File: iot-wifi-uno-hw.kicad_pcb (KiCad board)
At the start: 2 copper layers, 68.6 x 53.3 mm, 0 parts

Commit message: final schematic
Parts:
- added U1: usb_mini_b, Connectors:USB_Micro-B, F.Cu at (114.3, 74.9)
- added U2: NCP1117ST33T3G_MountingTab, TO_SOT_Packages_SMD:SOT-223, F.Cu at (133.3, 95.9)
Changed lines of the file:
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@@
-(kicad_pcb (version 20160815) (host pcbnew no-vcs-found-undefined)
+(kicad_pcb (version 20160815) (host pcbnew 201611122049+7349~55~ubuntu16.04.1)
   (general
-    (links 0)
-    (no_connects 0)
-    (area 105.969999 29.407502 174.700001 118.439001)
+    (links 6)
+    (no_connects 6)
+    (area 109.471337 58.578471 178.201339 112.068473)
     (thickness 1.6)
     (drawings 949)
     (tracks 0)
     (zones 0)
-    (modules 0)
-    (nets 1)
+    (modules 2)
+    (nets 3)
   )
   (page A4)
@@
   )
   (net 0 "")
+  (net 1 XO)
+  (net 2 "Net-(C3-Pad1)")
   (net_class Default "This is the default net class."
     (clearance 0.2)
@@
     (diff_pair_gap 0.25)
     (diff_pair_width 0.2)
+    (add_net "Net-(C3-Pad1)")
+    (add_net XO)
+  )
+  (module Connectors:USB_Micro-B (layer F.Cu)
+    (at 114.3 74.93 270)
+    (descr "Micro USB Type B Receptacle")
+    (tags "USB USB_B USB_micro USB_OTG")
+    (attr smd)
+    (fp_text reference U1 (at 0 -3.45 270) (layer F.SilkS)
+      (effects (font (size 1 1) (thickness 0.15)))
+    )
+    (fp_text value usb_mini_b (at 0 4.8 270) (layer F.Fab)
+      (effects (font (size 1 1) (thickness 0.15)))
+    )
+    (fp_line (start -4.3509 3.81746) (end -4.3509 -2.58754) (layer F.SilkS) (width 0.15))
+    (fp_line (start 4.3491 2.58746) (end -4.3509 2.58746) (layer F.SilkS) (width 0.15))
+    (fp_line (start 4.3491 -2.58754) (end 4.3491 3.81746) (layer F.SilkS) (width 0.15))
+    (fp_line (start -4.3509 -2.58754) (end 4.3491 -2.58754) (layer F.SilkS) (width 0.15))
+    (fp_line (start -4.3509 3.81746) (end 4.3491 3.81746) (layer F.SilkS) (width 0.15))
+    (fp_line (start -4.6 4.05) (end -4.6 -2.8) (layer F.CrtYd) (width 0.05))
+    (fp_line (start 4.6 4.05) (end -4.6 4.05) (layer F.CrtYd) (width 0.05))
+    (fp_line (start 4.6 -2.8) (end 4.6 4.05) (layer F.CrtYd) (width 0.05))
+    (fp_line (start -4.6 -2.8) (end 4.6 -2.8) (layer F.CrtYd) (width 0.05))
+    (pad 6 thru_hole oval (at 3.4991 1.13746) (size 1.55 1) (drill oval 1.15 0.5) (layers *.Cu *.Mask)
+      (net 1 XO))
+    (pad 6 thru_hole oval (at -3.5009 1.13746) (size 1.55 1) (drill oval 1.15 0.5) (layers *.Cu *.Mask)
+      (net 1 XO))
+    (pad 6 thru_hole oval (at 2.4991 -1.56254) (size 0.95 1.25) (drill oval 0.55 0.85) (layers *.Cu *.Mask)
+      (net 1 XO))
+    (pad 6 thru_hole oval (at -2.5009 -1.56254) (size 0.95 1.25) (drill oval 0.55 0.85) (layers *.Cu *.Mask)
+      (net 1 XO))
+    (pad 5 smd rect (at 1.2991 -1.56254) (size 1.35 0.4) (layers F.Cu F.Paste F.Mask)
+      (net 1 XO))
+    (pad 4 smd rect (at 0.6491 -1.56254) (size 1.35 0.4) (layers F.Cu F.Paste F.Mask))
+    (pad 3 smd rect (at -0.0009 -1.56254) (size 1.35 0.4) (layers F.Cu F.Paste F.Mask))
+    (pad 2 smd rect (at -0.6509 -1.56254) (size 1.35 0.4) (layers F.Cu F.Paste F.Mask))
+    (pad 1 smd rect (at -1.3009 -1.56254) (size 1.35 0.4) (layers F.Cu F.Paste F.Mask))
+  )
+  (module TO_SOT_Packages_SMD:SOT-223 (layer F.Cu)
+    (at 133.35 95.885 90)
+    (descr "module CMS SOT223 4 pins")
+    (tags "CMS SOT")
+    (attr smd)
+    (fp_text reference U2 (at 0 -0.762 90) (layer F.SilkS)
+      (effects (font (size 1 1) (thickness 0.15)))
+    )
+    (fp_text value NCP1117ST33T3G_MountingTab (at 0 0.762 90) (layer F.Fab)
+      (effects (font (size 1 1) (thickness 0.15)))
+    )
+    (fp_line (start 3.556 -2.286) (end 3.556 -1.524) (layer F.SilkS) (width 0.15))
+    (fp_line (start 2.032 -4.572) (end 3.556 -2.286) (layer F.SilkS) (width 0.15))
+    (fp_line (start -2.032 -4.572) (end 2.032 -4.572) (layer F.SilkS) (width 0.15))
+    (fp_line (start -3.556 -2.286) (end -2.032 -4.572) (layer F.SilkS) (width 0.15))
+    (fp_line (start -3.556 -1.524) (end -3.556 -2.286) (layer F.SilkS) (width 0.15))
+    (fp_line (start 3.556 4.572) (end 3.556 1.524) (layer F.SilkS) (width 0.15))
+    (fp_line (start -3.556 4.572) (end 3.556 4.572) (layer F.SilkS) (width 0.15))
+    (fp_line (start -3.556 1.524) (end -3.556 4.572) (layer F.SilkS) (width 0.15))
+    (pad 1 smd rect (at -2.286 3.302 90) (size 1.016 2.032) (layers F.Cu F.Paste F.Mask)
+      (net 1 XO))
+    (pad 3 smd rect (at 2.286 3.302 90) (size 1.016 2.032) (layers F.Cu F.Paste F.Mask))
+    (pad 2 smd rect (at 0 3.302 90) (size 1.016 2.032) (layers F.Cu F.Paste F.Mask)
+      (net 2 "Net-(C3-Pad1)"))
+    (pad 4 smd rect (at 0 -3.302 90) (size 3.6576 2.032) (layers F.Cu F.Paste F.Mask)
+      (net 2 "Net-(C3-Pad1)"))
+    (model TO_SOT_Packages_SMD.3dshapes/SOT-223.wrl
+      (at (xyz 0 0 0))
+      (scale (xyz 0.4 0.4 0.4))
+      (rotate (xyz 0 0 0))
+    )
   )
   (gr_circle (center 124.786338 61.193472) (end 124.659338 59.542472) (layer Edge.Cuts) (width 0.15))

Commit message: add PCB
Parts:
- added C1: 1uF/25V, Capacitors_SMD:C_1210_HandSoldering, F.Cu at (136.4, 91.5)
- added C10: 100nF, ESP8266:C_0603, F.Cu at (129.1, 82.6)
- added C11: 10uF/50V, Capacitors_SMD:C_1210_HandSoldering, F.Cu at (116.6, 95.9)
- added C12: 10uF/50V, Capacitors_SMD:C_1210_HandSoldering, F.Cu at (119.8, 95.9)
- added C13: 1uF, ESP8266:C_0603, F.Cu at (124.1, 92.3)
- added C14: 100nF, ESP8266:C_0603, F.Cu at (124.0, 99.4)
- added C15: 10uF/25V, Capacitors_SMD:C_1210_HandSoldering, F.Cu at (129.2, 99.2)
- added C16: 10uF/25V, Capacitors_SMD:C_1210_HandSoldering, F.Cu at (129.2, 92.5)
- added C2: 470pF, ESP8266:C_0603, F.Cu at (170.9, 77.9)
- added C3: 1uF/25V, Capacitors_SMD:C_1210_HandSoldering, F.Cu at (136.4, 100.1)
- added C4: 8pF, ESP8266:C_0603, F.Cu at (118.7, 71.5)
- added C5: 8pF, ESP8266:C_0603, F.Cu at (124.4, 71.5)
- added C6: 100nF, ESP8266:C_0603, F.Cu at (126.1, 71.5)
- added C7: 10uF/25v, Capacitors_SMD:C_1210_HandSoldering, F.Cu at (149.1, 82.4)
- added C8: 100nF, ESP8266:C_0603, F.Cu at (151.6, 82.4)
- added C9: 10uF, ESP8266:C_0603, F.Cu at (129.1, 84.0)
- added CON1: BARREL_JACK, Connectors:BARREL_JACK, F.Cu at (113.6, 104.5)
- added D1: L_PWR, LEDs:LED_0603, F.Cu at (147.4, 88.5)
- added D2: N5819/SS14/S4(SOD_323), ESP8266:do214aa, F.Cu at (112.1, 85.0)
- added D3: LED_Blue, LEDs:LED_0603, F.Cu at (147.4, 93.1)
- added D4: D, ESP8266:do214aa, F.Cu at (112.1, 95.9)
- added L1: 22uF, Choke_SMD:Choke_SMD_Wuerth-WE-PD2-Typ-MS, F.Cu at (129.2, 105.6)
- added P1: CONN_01X08, Pin_Headers:Pin_Header_Straight_1x08, F.Cu at (154.9, 61.0)
- added P2: CONN_01X08, Pin_Headers:Pin_Header_Straight_1x08, F.Cu at (137.2, 109.2)
- added P3: CONN_01X06, Pin_Headers:Pin_Header_Straight_1x06, F.Cu at (160.0, 109.2)
- added P4: CONN_01X10, Pin_Headers:Pin_Header_Straight_1x10, F.Cu at (127.0, 61.0)
- added P5: CONN_01X04, Pin_Headers:Pin_Header_Straight_1x04, F.Cu at (116.9, 88.8)
- added Q1: Q_NPN_CBE, TO_SOT_Packages_SMD:SOT-323, F.Cu at (133.2, 81.0)
- added Q2: Q_NPN_CBE, TO_SOT_Packages_SMD:SOT-323, F.Cu at (133.2, 74.6)
- added R1: 12k, ESP8266:R_0603, F.Cu at (161.1, 101.8)
- added R10: 470R, ESP8266:R_0603, F.Cu at (129.1, 71.5)
- added R11: 470R, ESP8266:R_0603, F.Cu at (147.4, 91.6)
- added R12: 0R, ESP8266:R_0603, F.Cu at (163.3, 77.9)
- added R13: 12K, ESP8266:R_0603, F.Cu at (134.0, 77.8)
- added R14: 12K, ESP8266:R_0603, F.Cu at (132.4, 77.8)
- added R15: 52.5K, ESP8266:R_0603, F.Cu at (128.2, 95.8)
- added R16: 10k, ESP8266:R_0603, F.Cu at (126.6, 95.8)
- added R17: 470R, ESP8266:R_0603, F.Cu at (172.4, 77.9)
- added R18: 470R, ESP8266:R_0603, F.Cu at (162.6, 101.8)
- added R19: 3K/1%, ESP8266:R_0603, F.Cu at (141.1, 97.3)
- added R2: 12k, ESP8266:R_0603, F.Cu at (159.1, 101.9)
- added R20: 1K/1%, ESP8266:R_0603, F.Cu at (141.1, 94.1)
- added R3: 12k, ESP8266:R_0603, F.Cu at (164.8, 77.9)
- added R4: 12k, ESP8266:R_0603, F.Cu at (169.4, 77.9)
- added R5: 12k, ESP8266:R_0603, F.Cu at (157.0, 101.7)
- added R6: 220k/1%, ESP8266:R_0603, F.Cu at (167.9, 77.9)
- added R7: 100k/1%, ESP8266:R_0603, F.Cu at (166.3, 77.9)
- added R8: 470R, ESP8266:R_0603, F.Cu at (147.4, 90.1)
- added R9: 470R, ESP8266:R_0603, F.Cu at (127.6, 71.5)
- added SW1: REST, Buttons_Switches_SMD:SW_SPST_FSMSM, F.Cu at (116.2, 61.6)
- added SW2: GPIO0, Buttons_Switches_SMD:SW_SPST_FSMSM, F.Cu at (116.2, 67.4)
- added U3: MCP16311-MS, Housings_SSOP:MSOP-8-1EP_3x3mm_Pitch0.65mm, F.Cu at (124.0, 95.8)
- added U4: CH340G, Housings_SOIC:SOIC-16_3.9x9.9mm_Pitch1.27mm, F.Cu at (125.5, 77.8)
- added U5: ESP-12E, ESP8266:ESP-12F, F.Cu at (169.1, 83.8)
- added X1: CRYSTAL_ABM3C, ESP8266:Crystal_SMD_3225_4Pads, F.Cu at (121.5, 71.5)
- U2: value NCP1117ST33T3G_MountingTab -> BD00GA5WEFJ; footprint TO_SOT_Packages_SMD:SOT-223 -> ESP8266:HTSOP-J8
- moved U2 5.54 mm to (138.3, 98.3)
- moved U1 0.90 mm to (113.7, 74.3)
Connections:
- U1 pad 1: (no net) -> VCC
- U1 pad 2: (no net) -> D-
- U1 pad 3: (no net) -> D+
- U1 pad 5: XO -> GND
- U1 pad 6: XO -> GND
- U2 pad 1: XO -> +3V3
- U2 pad 2: Net-(C3-Pad1) -> Net-(R19-Pad2)
- U2 pad 3: (no net) -> GND
- U2 pad 4: Net-(C3-Pad1) -> (no net)
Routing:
- net GPIO15: track 0.00 -> 47.2 mm, vias 0 -> 2
- net GPIO0: track 0.00 -> 43.2 mm, vias 0 -> 1
- net GPIO2: track 0.00 -> 41.6 mm, vias 0 -> 1
- net RXD: track 0.00 -> 39.2 mm, vias 0 -> 1
- net TXD: track 0.00 -> 39.0 mm, vias 0 -> 1
- net SCLK: track 0.00 -> 37.9 mm, vias 0 -> 1
- net GPIO14: track 0.00 -> 34.8 mm
- net MOSI: track 0.00 -> 34.8 mm, vias 0 -> 1
- net GPIO12: track 0.00 -> 32.6 mm, vias 0 -> 1
- net GPIO10: track 0.00 -> 32.5 mm, vias 0 -> 1
- net CSO: track 0.00 -> 31.2 mm, vias 0 -> 1
- net MISO: track 0.00 -> 30.5 mm, vias 0 -> 1
- net GPIO13: track 0.00 -> 29.6 mm, vias 0 -> 1
- net GPIO09: track 0.00 -> 26.5 mm, vias 0 -> 1
- net GPIO16: track 0.00 -> 26.3 mm
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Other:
- net class Default: clearance 0.2 -> 0.5
- rule trace_clearance: 0.2 -> 0.5

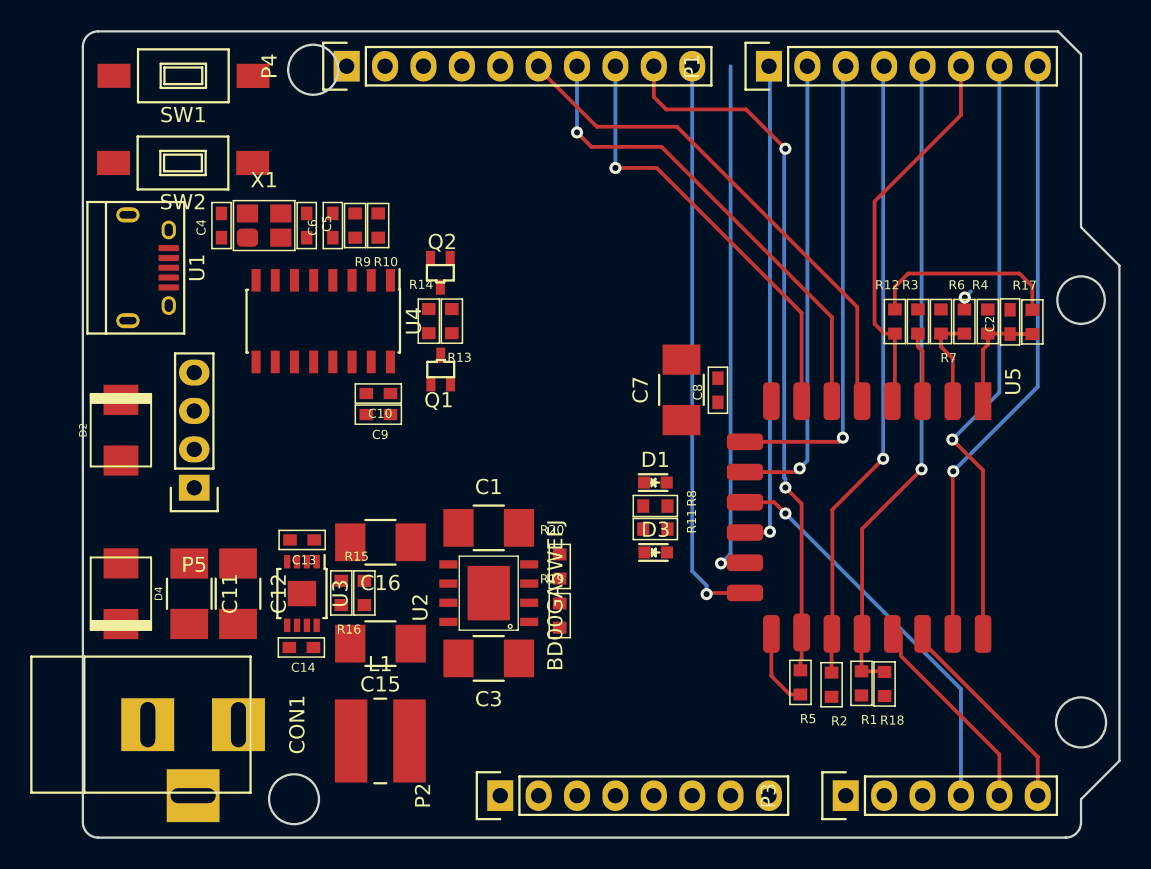
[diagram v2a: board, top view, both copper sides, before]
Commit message: add VIN to PCB - MOSFET & OpAmp
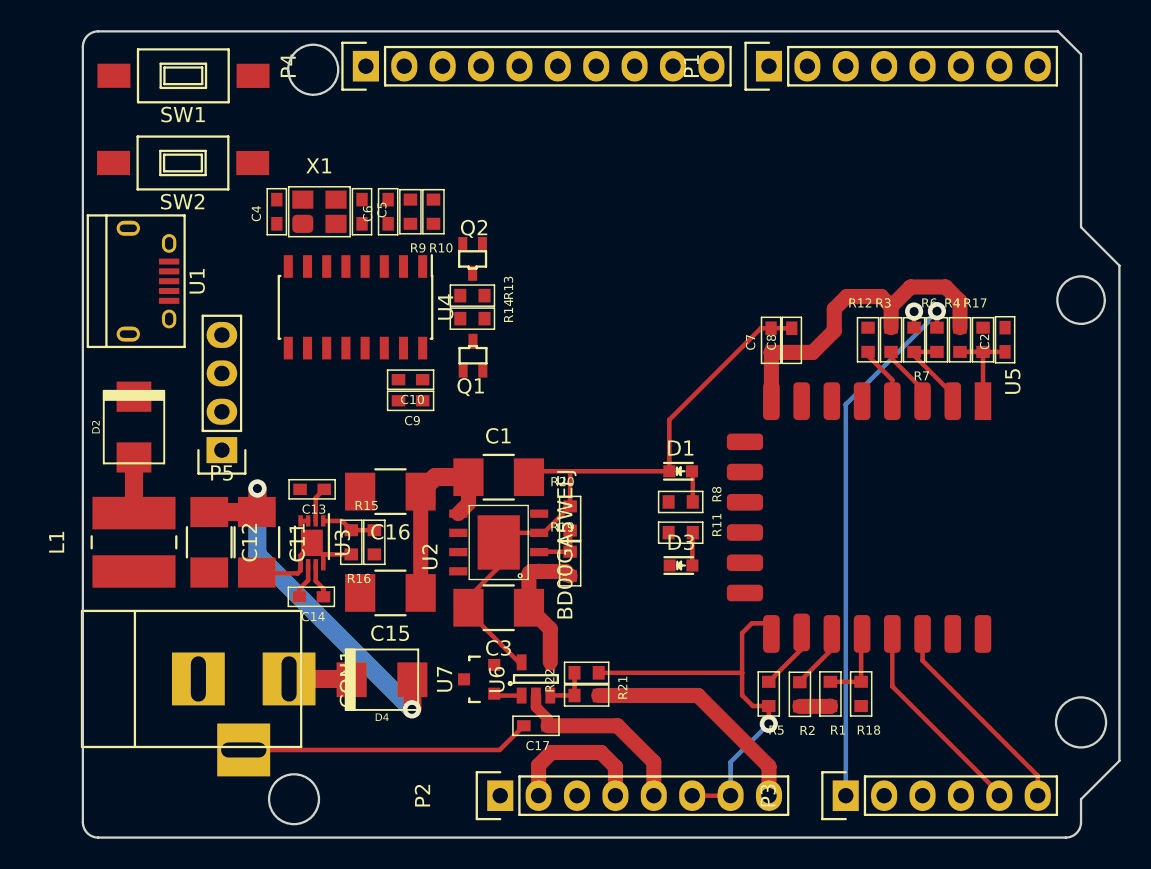
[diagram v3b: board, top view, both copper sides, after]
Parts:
- added C17: 100nF, ESP8266:C_0603, F.Cu at (139.5, 104.6)
- added R21: 10k, ESP8266:R_0603, F.Cu at (142.9, 102.6)
- added R22: 10k, ESP8266:R_0603, F.Cu at (142.9, 101.1)
- added U6: MCP6001R, TO_SOT_Packages_SMD:SOT-23-5, F.Cu at (139.5, 101.5)
- added U7: MOSFET-P, TO_SOT_Packages_SMD:SOT-23, F.Cu at (135.8, 101.5)
- C7: footprint Capacitors_SMD:C_1210_HandSoldering -> ESP8266:C_0603
- D2: value N5819/SS14/S4(SOD_323) -> ss24
- U3: value MCP16311-MS -> MCP16311-MNY; footprint Housings_SSOP:MSOP-8-1EP_3x3mm_Pitch0.65mm -> Housings_DFN_QFN:DFN-8-1EP_3x2mm_Pitch0.5mm
- moved L1 20.9 mm to (112.9, 92.5), turned to 90 degrees
- moved D4 18.2 mm to (129.3, 101.5), turned to 180 degrees
- moved C7 6.78 mm to (155.1, 79.1)
- moved P5 6.56 mm to (118.7, 82.5)
- moved C8 5.90 mm to (156.5, 79.1)
- moved C11 5.62 mm to (121.1, 92.5)
- moved CON1 4.51 mm to (117.0, 101.5)
- moved C12 3.90 mm to (117.9, 92.5)
- moved C4 3.77 mm to (122.4, 70.6)
- moved C6 3.77 mm to (129.7, 70.6)
- moved R10 3.77 mm to (132.7, 70.6)
- moved X1 3.77 mm to (125.2, 70.6)
- moved C5 3.77 mm to (128.0, 70.6)
- moved R9 3.77 mm to (131.2, 70.6)
- moved R19 3.50 mm to (141.8, 93.9)
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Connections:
- C11 pad 1: Net-(C11-Pad1) -> Vin
- C12 pad 1: Net-(C11-Pad1) -> Vin
- D4 pad 1: Net-(C11-Pad1) -> Vin
- P2 pad 8: (no net) -> Vin
- U3 pad 3: Net-(C11-Pad1) -> Vin
- U3 pad 4: Net-(C11-Pad1) -> Vin
- U3 pad 9: (no net) -> GND
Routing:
- net GND: track 5.91 -> 99.3 mm, vias 0 -> 2
- net +3V3: track 0.00 -> 44.3 mm
- net GPIO15: track 47.2 -> 4.77 mm, vias 2 -> 0
- net Vin: track 0.00 -> 41.2 mm, vias 0 -> 2
- net RXD: track 39.2 -> 0.00 mm, vias 1 -> 0
- net TXD: track 39.0 -> 0.00 mm, vias 1 -> 0
- net SCLK: track 37.9 -> 0.00 mm, vias 1 -> 0
- net GPIO0: track 43.2 -> 5.93 mm, vias 1 -> 0
- net GPIO2: track 41.6 -> 4.77 mm, vias 1 -> 0
- net GPIO14: track 34.8 -> 0.00 mm
- net MOSI: track 34.8 -> 0.00 mm, vias 1 -> 0
- net ADC_EX: track 1.36 -> 35.6 mm
- net GPIO12: track 32.6 -> 0.00 mm, vias 1 -> 0
- net GPIO10: track 32.5 -> 0.00 mm, vias 1 -> 0
- net CSO: track 31.2 -> 0.00 mm, vias 1 -> 0
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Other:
- net class Default: clearance 0.5 -> 0.1; trace_width 0.25 -> 0.3; via_dia 0.8 -> 1.2; via_drill 0.4 -> 0.6
- rule trace_clearance: 0.5 -> 0.1

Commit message: Completed PCB
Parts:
- removed SW1: REST, Buttons_Switches_SMD:SW_SPST_FSMSM
- removed SW2: GPIO0, Buttons_Switches_SMD:SW_SPST_FSMSM
- added GPIO0: GPIO0, ESP8266:Tact_Switch_TS6X3.6, F.Cu at (112.4, 63.9)
- added RST1: REST, ESP8266:Tact_Switch_TS6X3.6, F.Cu at (119.0, 63.9)
- moved P5 6.10 mm to (112.8, 83.8)
- moved D2 4.86 mm to (117.7, 83.8)
- moved U1 1.78 mm to (113.5, 73.4)
- moved L1 1.53 mm to (113.0, 94.0)
- moved CON1 1.17 mm to (116.6, 102.6)
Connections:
- P2 pad 2: +3V3 -> (no net)
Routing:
- net GND: track 99.3 -> 284.9 mm, vias 2 -> 14
- net GPIO5: track 14.6 -> 111.3 mm, vias 0 -> 4
- net +3V3: track 44.3 -> 137.6 mm, vias 0 -> 5
- net GPIO4: track 14.3 -> 105.6 mm, vias 0 -> 2
- net REST: track 6.95 -> 89.2 mm, vias 0 -> 2
- net TXD: track 0.00 -> 81.1 mm, vias 0 -> 3
- net RXD: track 0.00 -> 81.0 mm, vias 0 -> 2
- net Net-(GPIO0-Pad1): track 0.00 -> 76.8 mm, vias 0 -> 2
- net GPIO0: track 5.93 -> 77.3 mm, vias 0 -> 3
- net Net-(R12-Pad2): track 0.00 -> 70.2 mm, vias 0 -> 4
- net +5V: track 29.2 -> 87.9 mm, vias 0 -> 4
- net GPIO16: track 4.63 -> 58.2 mm, vias 0 -> 4
- net GPIO2: track 4.77 -> 56.3 mm
- net GPIO15: track 4.77 -> 55.1 mm, vias 0 -> 2
- net SCLK: track 0.00 -> 47.4 mm, vias 0 -> 2
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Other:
- net class Default: clearance 0.1 -> 0.3; trace_width 0.3 -> 1
- rule trace_clearance: 0.1 -> 0.3
- board text added: "3.3V"
- board text added: "5V"
- board text added: "ADC"
- board text added: "CSO"
- board text added: "GND"
- board text added: "GPIO0"
- board text added: "GPIO02"
- board text added: "GPIO04"
- board text added: "GPIO05"
- board text added: "GPIO09"
- board text added: "GPIO10"
- board text added: "GPIO12"
- board text added: "GPIO13"
- board text added: "GPIO14"
- board text added: "GPIO15"
- board text added: "GPIO16"
- board text added: "MISO"
- board text added: "MOSI"
- board text added: "OLED"
- board text added: "PWR"
- board text added: "RST"
- board text added: "RXD"
- board text added: "SCL"
- board text added: "SCLK"
- board text added: "SDA"
- board text added: "TXD"
- board text added: "VIN"

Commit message: completed PCB
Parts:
- added G***: LOGO, ESP8266:logo_cc-bby-sa_6.7x5mm, F.Cu at (165.7, 73.7)
- added G***: LOGO, ESP8266:logo_openhardware_5.7x6.1mm, F.Cu at (154.0, 73.7)
- added G***: LOGO, ESP8266:logo_iotmake_7.5x6.5mm, F.Cu at (143.8, 73.7)
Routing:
- net TXD: track 81.1 -> 83.2 mm
- net MISO: track 30.7 -> 32.7 mm
- net GPIO5: track 111.3 -> 113.3 mm
- net GPIO4: track 105.6 -> 106.7 mm
- net REST: track 89.2 -> 88.3 mm
- net Net-(GPIO0-Pad1): track 76.8 -> 75.8 mm
- net GPIO2: track 56.3 -> 55.3 mm
- net +5V: track 87.9 -> 87.2 mm
- net Net-(Q1-Pad3): track 8.35 -> 9.06 mm
- added copper zone on B.Cu, net GND
- added copper zone on F.Cu, net GND
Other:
- net class Default: trace_width 1 -> 0.3
- board text added: "https://esp8266.vn/"
